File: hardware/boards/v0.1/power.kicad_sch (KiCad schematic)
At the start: 65 parts, among them IC3 SP3401-02UTG, J2 USB, U20 TPS62A02DRL, U23 BQ21040DBV, U30 FUSB307BMPX, U31 TPS22929D, U32 LTC2942, U36 STM6601GU2BDM6F, U39 TPS61252DSG, U40 MIC2017YM6

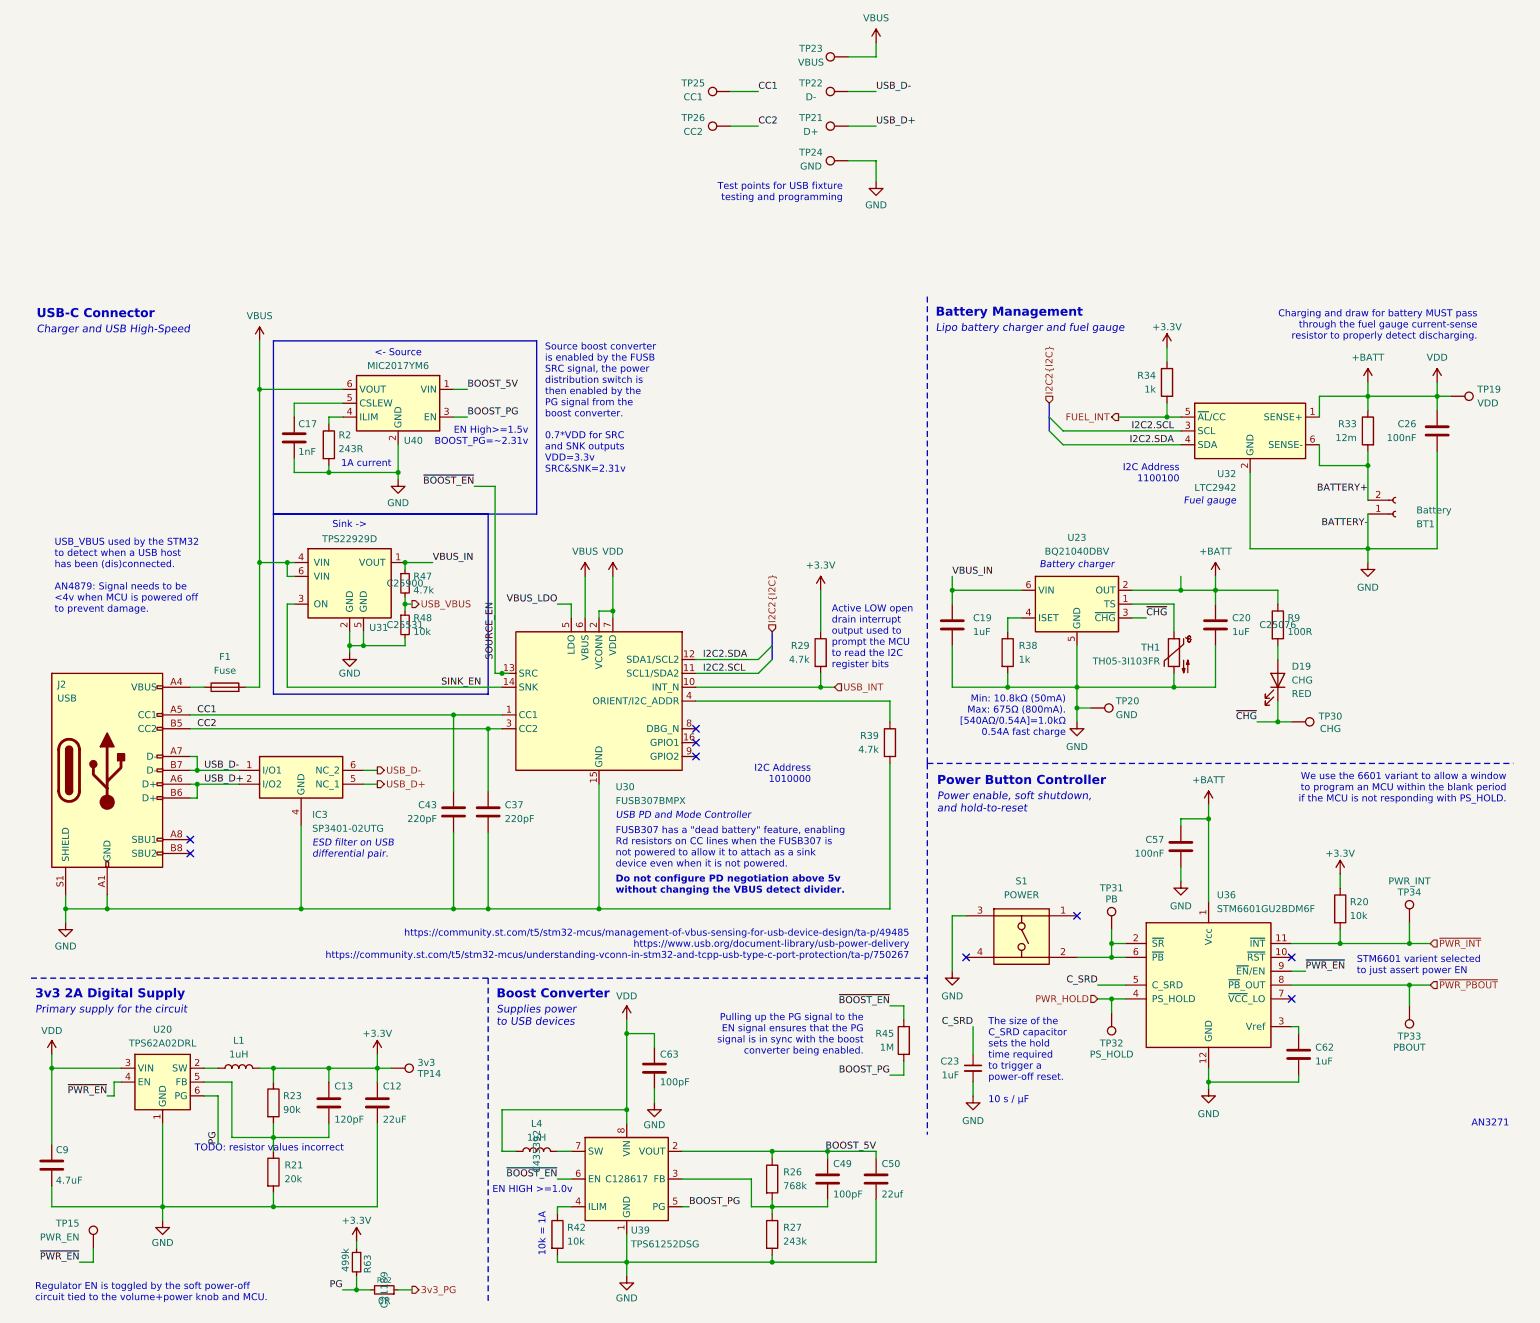
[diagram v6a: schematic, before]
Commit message: feat: swap out of stock components
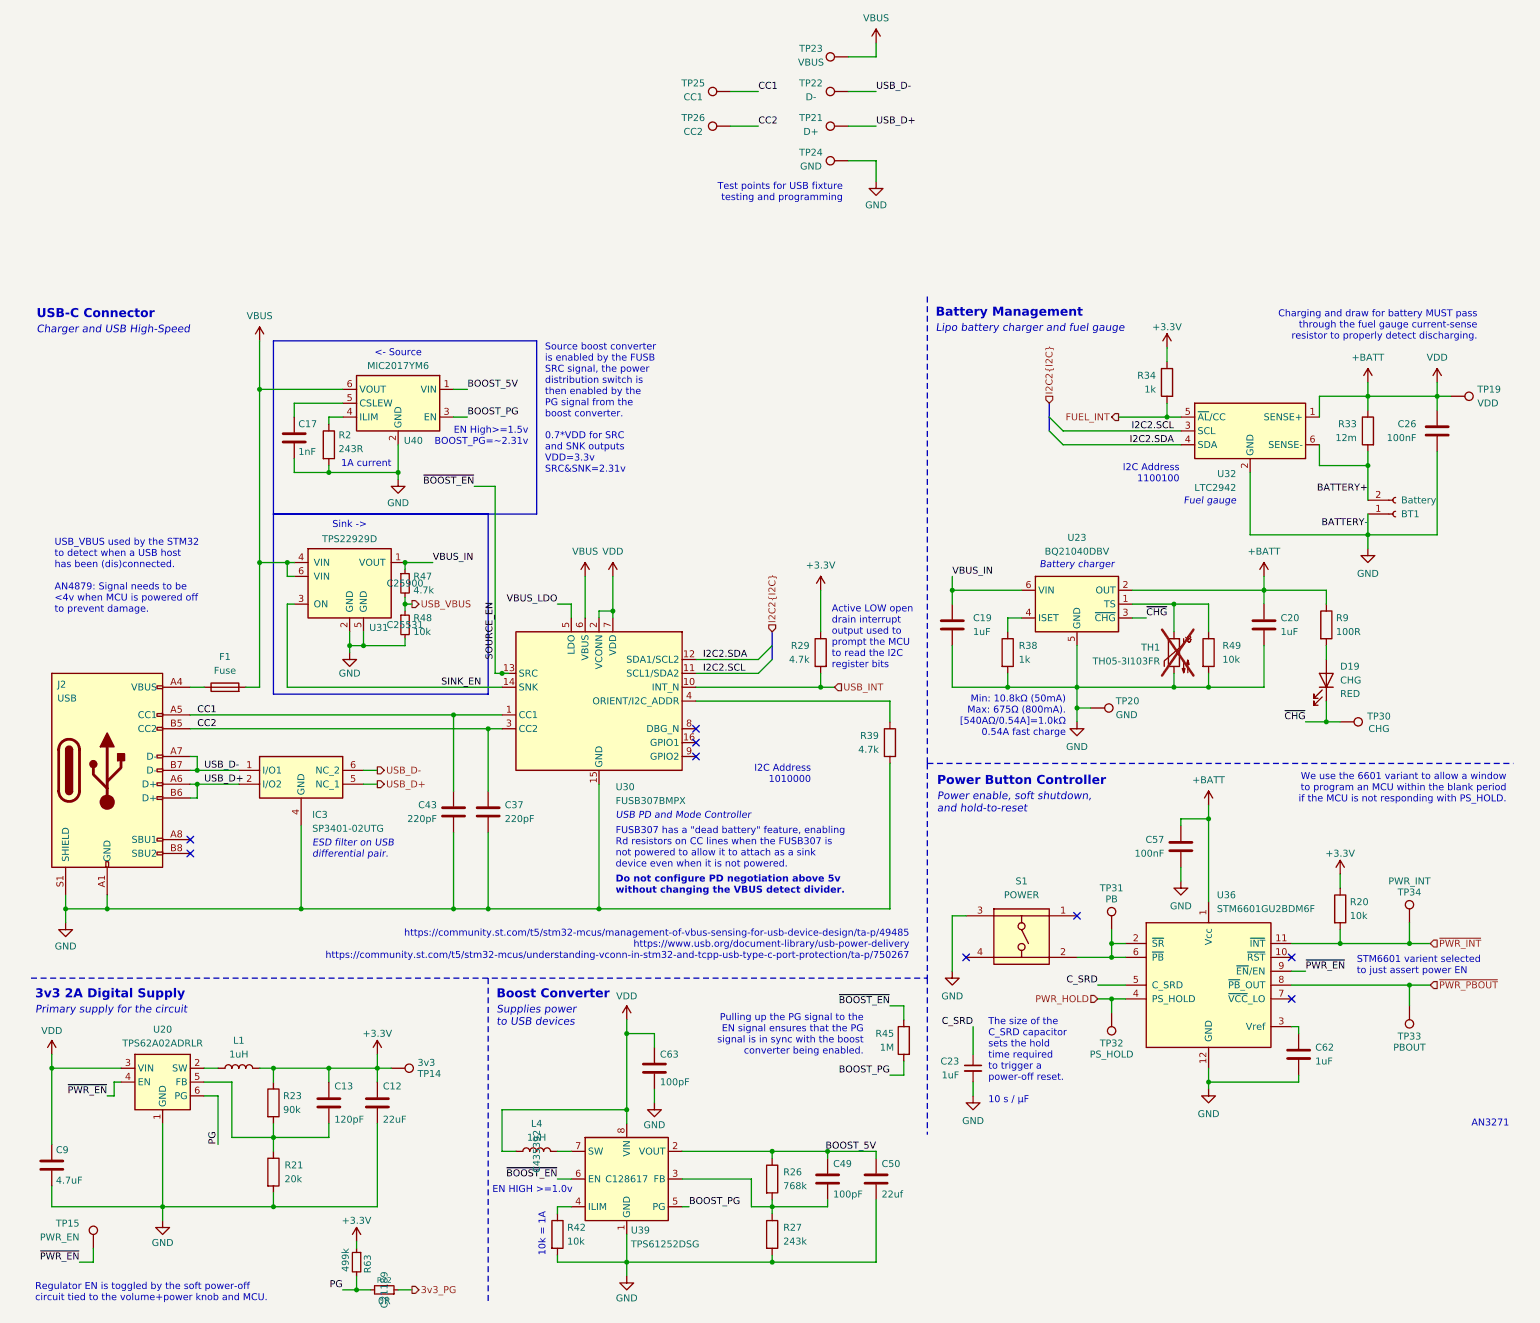
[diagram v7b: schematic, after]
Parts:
- added R49: 10k, Resistor_SMD:R_0805_2012Metric_Pad1.20x1.40mm_HandSolder, symbol Device:R
- IC3: Manufacturer_Name LITTELFUSE -> (none); Manufacturer_Part_Number SP3401-02UTG -> (none)
- R23: footprint Resistor_SMD:R_0805_2012Metric -> Resistor_SMD:R_1206_3216Metric; JLC C247028 -> C871504
- S1: Manufacturer_Name Wurth Elektronik -> (none); Manufacturer_Part_Number 436331045822 -> (none)
- TH1: now not fitted; now left out of the parts list
- U20: value TPS62A02DRL -> TPS62A02ADRLR; symbol Regulator_Switching:TPS62A02DRL -> Regulator_Switching:TPS62A02ADRL; JLC C5350187 -> C5820994
- U23: JLC C78978 -> C202311
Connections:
- net GND: now also R49.2
- net at TH1.1, U23.1 (TS): now also R49.1
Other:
- note removed: "TODO: resistor values incorrect"
- moved on the sheet: C20, D19, R9, TP30

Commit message: feat: various cleanup and BOM adjustment, split audio in into two switches
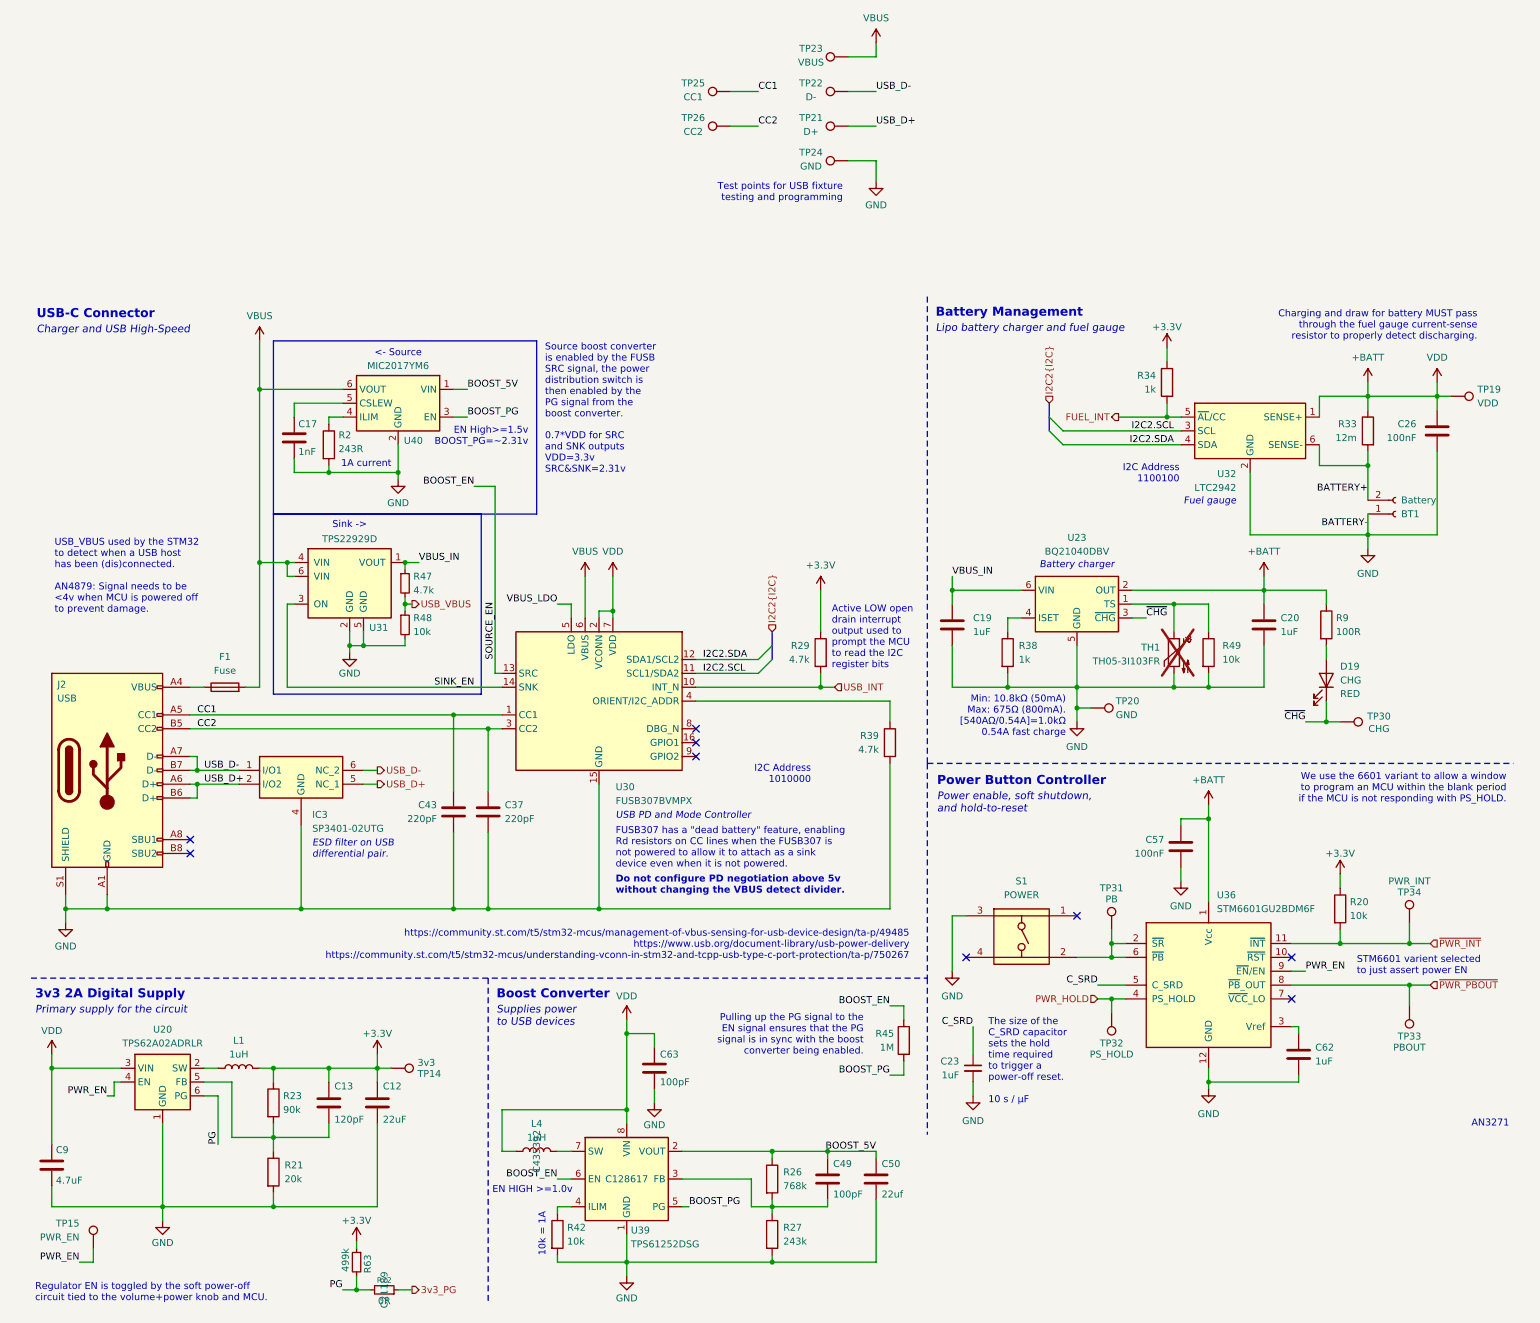
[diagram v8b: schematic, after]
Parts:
- U30: value FUSB307BMPX -> FUSB307BVMPX
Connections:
- net SOURCE_EN renamed BOOST_EN
- net ~{PWR_EN} renamed PWR_EN
